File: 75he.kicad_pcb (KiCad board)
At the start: 2 copper layers, 317.6 x 131.8 mm, 391 parts, among them J201 Connector, USB-TYPE-C-16P, K1 DRV5055A3xDBZxQ1, K10 DRV5055A3xDBZxQ1, K11 DRV5055A3xDBZxQ1, K12 DRV5055A3xDBZxQ1, K13 DRV5055A3xDBZxQ1, K14 DRV5055A3xDBZxQ1, K15 DRV5055A3xDBZxQ1, K16 DRV5055A3xDBZxQ1, K17 DRV5055A3xDBZxQ1, K18 DRV5055A3xDBZxQ1, K19 DRV5055A3xDBZxQ1, K2 DRV5055A3xDBZxQ1, K20 DRV5055A3xDBZxQ1, K21 DRV5055A3xDBZxQ1, K22 DRV5055A3xDBZxQ1, K23 DRV5055A3xDBZxQ1, K24 DRV5055A3xDBZxQ1, K25 DRV5055A3xDBZxQ1, K26 DRV5055A3xDBZxQ1, K27 DRV5055A3xDBZxQ1, K28 DRV5055A3xDBZxQ1, K29 DRV5055A3xDBZxQ1, K3 DRV5055A3xDBZxQ1, K30 DRV5055A3xDBZxQ1, K31 DRV5055A3xDBZxQ1, K32 DRV5055A3xDBZxQ1, K33 DRV5055A3xDBZxQ1, K34 DRV5055A3xDBZxQ1, K35 DRV5055A3xDBZxQ1, K36 DRV5055A3xDBZxQ1, K37 DRV5055A3xDBZxQ1, K38 DRV5055A3xDBZxQ1, K39 DRV5055A3xDBZxQ1, K4 DRV5055A3xDBZxQ1, K40 DRV5055A3xDBZxQ1, K41 DRV5055A3xDBZxQ1, K42 DRV5055A3xDBZxQ1, K43 DRV5055A3xDBZxQ1, K44 DRV5055A3xDBZxQ1, K45 DRV5055A3xDBZxQ1, K46 DRV5055A3xDBZxQ1, K47 DRV5055A3xDBZxQ1, K48 DRV5055A3xDBZxQ1, K49 DRV5055A3xDBZxQ1, K5 DRV5055A3xDBZxQ1, K50 DRV5055A3xDBZxQ1, K51 DRV5055A3xDBZxQ1, K52 DRV5055A3xDBZxQ1, K53 DRV5055A3xDBZxQ1, K54 DRV5055A3xDBZxQ1, K55 DRV5055A3xDBZxQ1, K56 DRV5055A3xDBZxQ1, K57 DRV5055A3xDBZxQ1, K58 DRV5055A3xDBZxQ1, K59 DRV5055A3xDBZxQ1, K6 DRV5055A3xDBZxQ1, K60 DRV5055A3xDBZxQ1, K61 DRV5055A3xDBZxQ1, K62 DRV5055A3xDBZxQ1, K63 DRV5055A3xDBZxQ1, K64 DRV5055A3xDBZxQ1, K65 DRV5055A3xDBZxQ1, K66 DRV5055A3xDBZxQ1, K67 DRV5055A3xDBZxQ1, K68 DRV5055A3xDBZxQ1, K69 DRV5055A3xDBZxQ1, K7 DRV5055A3xDBZxQ1, K70 DRV5055A3xDBZxQ1, K71 DRV5055A3xDBZxQ1, K72 DRV5055A3xDBZxQ1, K73 DRV5055A3xDBZxQ1, K74 DRV5055A3xDBZxQ1, K75 DRV5055A3xDBZxQ1, K76 DRV5055A3xDBZxQ1, K77 DRV5055A3xDBZxQ1, K78 DRV5055A3xDBZxQ1, K79 DRV5055A3xDBZxQ1, K8 DRV5055A3xDBZxQ1, K80 DRV5055A3xDBZxQ1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

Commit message: continue sensor out
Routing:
- net K53_OUT: track 0.00 -> 40.0 mm
- net K9_OUT: track 0.00 -> 38.0 mm
- net K56_OUT: track 0.00 -> 37.8 mm
- net K12_OUT: track 0.00 -> 31.0 mm
- net K54_OUT: track 0.00 -> 23.3 mm
- net K55_OUT: track 0.00 -> 22.2 mm
- net K10_OUT: track 0.00 -> 15.3 mm
- net K11_OUT: track 0.00 -> 12.7 mm
- net K14_OUT: track 0.00 -> 1.85 mm
- net K29_OUT: track 0.00 -> 1.84 mm
- net K24_OUT: track 0.00 -> 1.82 mm
- net K13_OUT: track 0.00 -> 1.82 mm
- net K28_OUT: track 0.00 -> 1.81 mm
- net K37_OUT: track 24.9 -> 26.7 mm
- net K27_OUT: track 0.00 -> 1.80 mm
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
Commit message: continue sensor out
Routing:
- net K23_OUT: track 1.76 -> 64.6 mm, vias 0 -> 4
- net K24_OUT: track 1.82 -> 45.3 mm, vias 0 -> 4
- net K25_OUT: track 1.80 -> 30.6 mm, vias 0 -> 4

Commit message: continue sensor out
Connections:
- M3 pad 1: unconnected-(M3-Y4-Pad1) -> K29_OUT
- M3 pad 12: unconnected-(M3-Y3-Pad12) -> K13_OUT
- M3 pad 15: unconnected-(M3-Y2-Pad15) -> K14_OUT
- M3 pad 2: unconnected-(M3-Y6-Pad2) -> K28_OUT
- M3 pad 4: unconnected-(M3-Y7-Pad4) -> K27_OUT
- M3 pad 5: unconnected-(M3-Y5-Pad5) -> K26_OUT

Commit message: start sensors power rail
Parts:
- C101, C102, C103, C104, C105, C11, C111, C112, C113, C114, C115, C121, C122, C123, C124, C125, C13, C131, C132, C133, C134, C135, C141, C142, C143, C144, C145, C15, C151, C153, C154, C155, C161, C163, C17, C19, C21, C23, C25, C27, C29, C31, C35, C37, C39, C41, C43, C45, C47, C49, C5, C51, C53, C55, C57, C59, C61, C65, C67, C69, C7, C71, C73, C75, C77, C79, C81, C82, C83, C84, C85, C9, C91, C92, C94, C95: moved to B.Cu
- moved C91 333.5 mm to (41.4, 135.9), turned to 0 degrees
- moved C61 313.4 mm to (65.1, 135.9), turned to 0 degrees
- moved C31 295.9 mm to (89.0, 135.9), turned to 0 degrees
- moved C47 281.9 mm to (329.6, 140.6), turned to 0 degrees
- moved C144 269.6 mm to (41.4, 116.9)
- moved C11 269.1 mm to (379.7, 104.5), turned to 180 degrees
- moved C13 269.1 mm to (379.7, 108.2), turned to 180 degrees
- moved C5 269.1 mm to (379.7, 93.4), turned to 180 degrees
- moved C7 269.1 mm to (379.7, 97.1), turned to 180 degrees
- moved C9 269.1 mm to (379.7, 100.8), turned to 180 degrees
- moved C77 266.9 mm to (310.5, 140.7), turned to 0 degrees
- moved C151 265.9 mm to (229.5, 135.9), turned to 0 degrees
- moved C19 265.1 mm to (376.8, 91.5), turned to 180 degrees
- moved C21 265.1 mm to (376.8, 95.2), turned to 180 degrees
- moved C23 265.1 mm to (376.8, 99.0), turned to 180 degrees
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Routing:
- net +3.3VA: track 473.5 -> 1042.3 mm, vias 8 -> 40
- net K26_OUT: track 1.78 -> 62.5 mm
- net K29_OUT: track 1.84 -> 50.6 mm
- net K27_OUT: track 1.80 -> 45.2 mm
- net K28_OUT: track 1.81 -> 33.5 mm
- net K13_OUT: track 1.82 -> 17.0 mm
- net K14_OUT: track 1.85 -> 14.5 mm
- net K74_OUT: track 25.3 -> 26.8 mm
- net K80_OUT: track 40.1 -> 41.6 mm
- net K77_OUT: track 41.5 -> 40.1 mm
- net K79_OUT: track 42.6 -> 43.3 mm

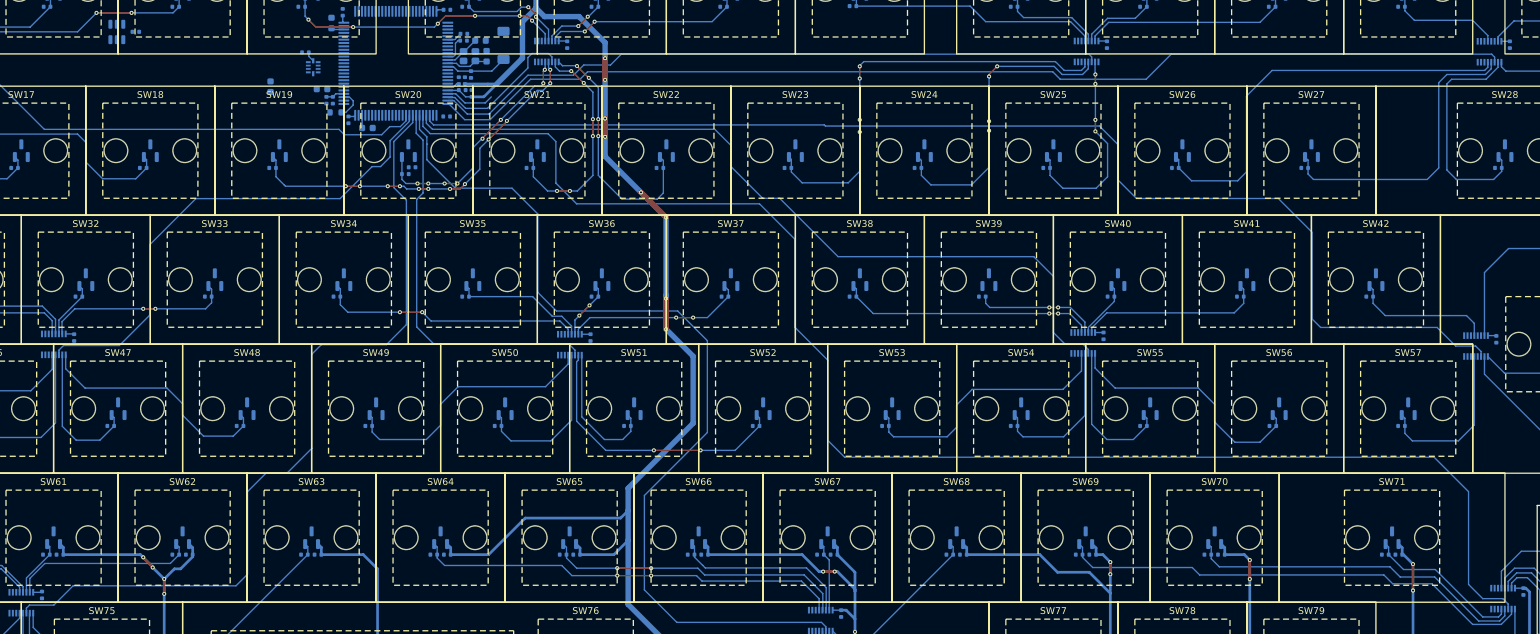
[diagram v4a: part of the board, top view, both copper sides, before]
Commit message: start sensors power rail
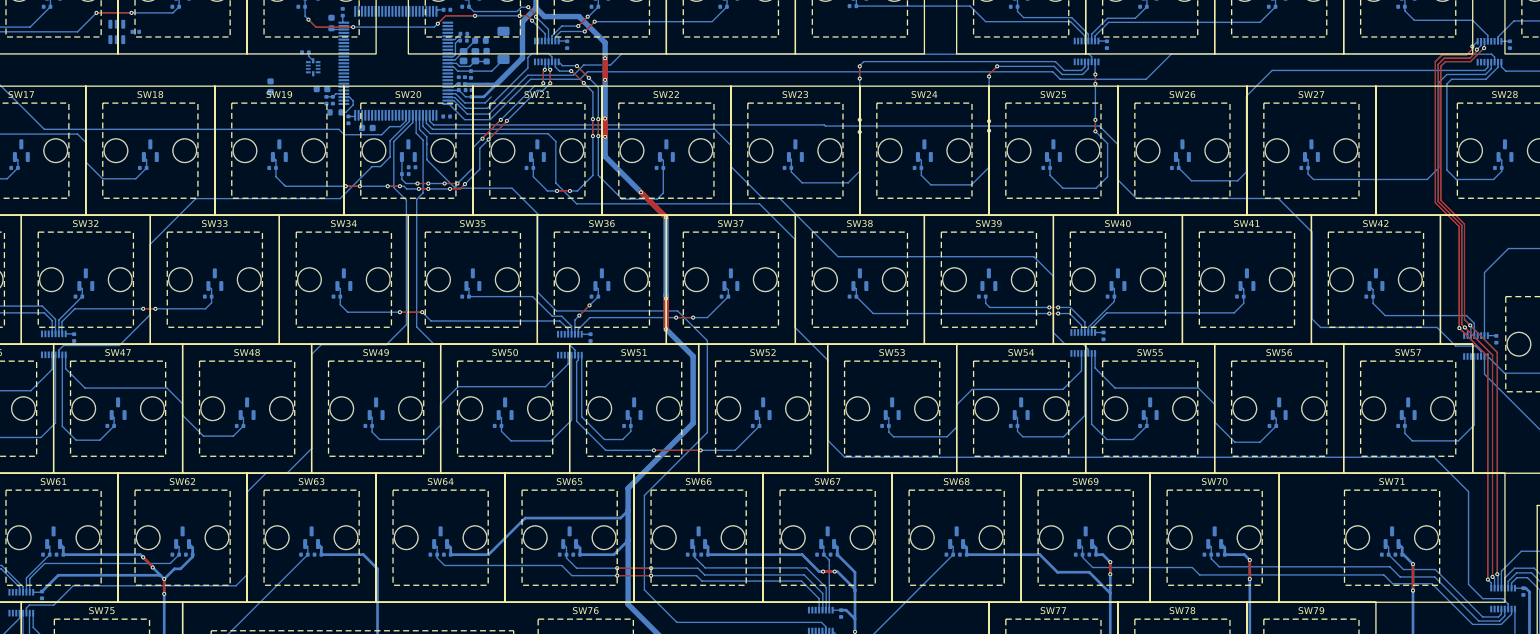
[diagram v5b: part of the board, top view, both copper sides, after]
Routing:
- net M_SEL_0: track 0.00 -> 90.6 mm, vias 0 -> 3
- net M_SEL_1: track 0.00 -> 90.4 mm, vias 0 -> 3
- net M_SEL_2: track 0.00 -> 90.3 mm, vias 0 -> 3
- net +3.3VA: track 1042.3 -> 1060.8 mm
